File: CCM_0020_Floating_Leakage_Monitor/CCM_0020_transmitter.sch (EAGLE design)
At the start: 61 parts, among them IC1 LMC6041, IC2 LT1494, IC3 LT1495, IC4 LTC1440, IC6 LT6656A-5.0V, Q1 SMP4117A, Q2 SMP4117A, Q3 SMP4117A, Q4 SMP4117A, T1 3904SM

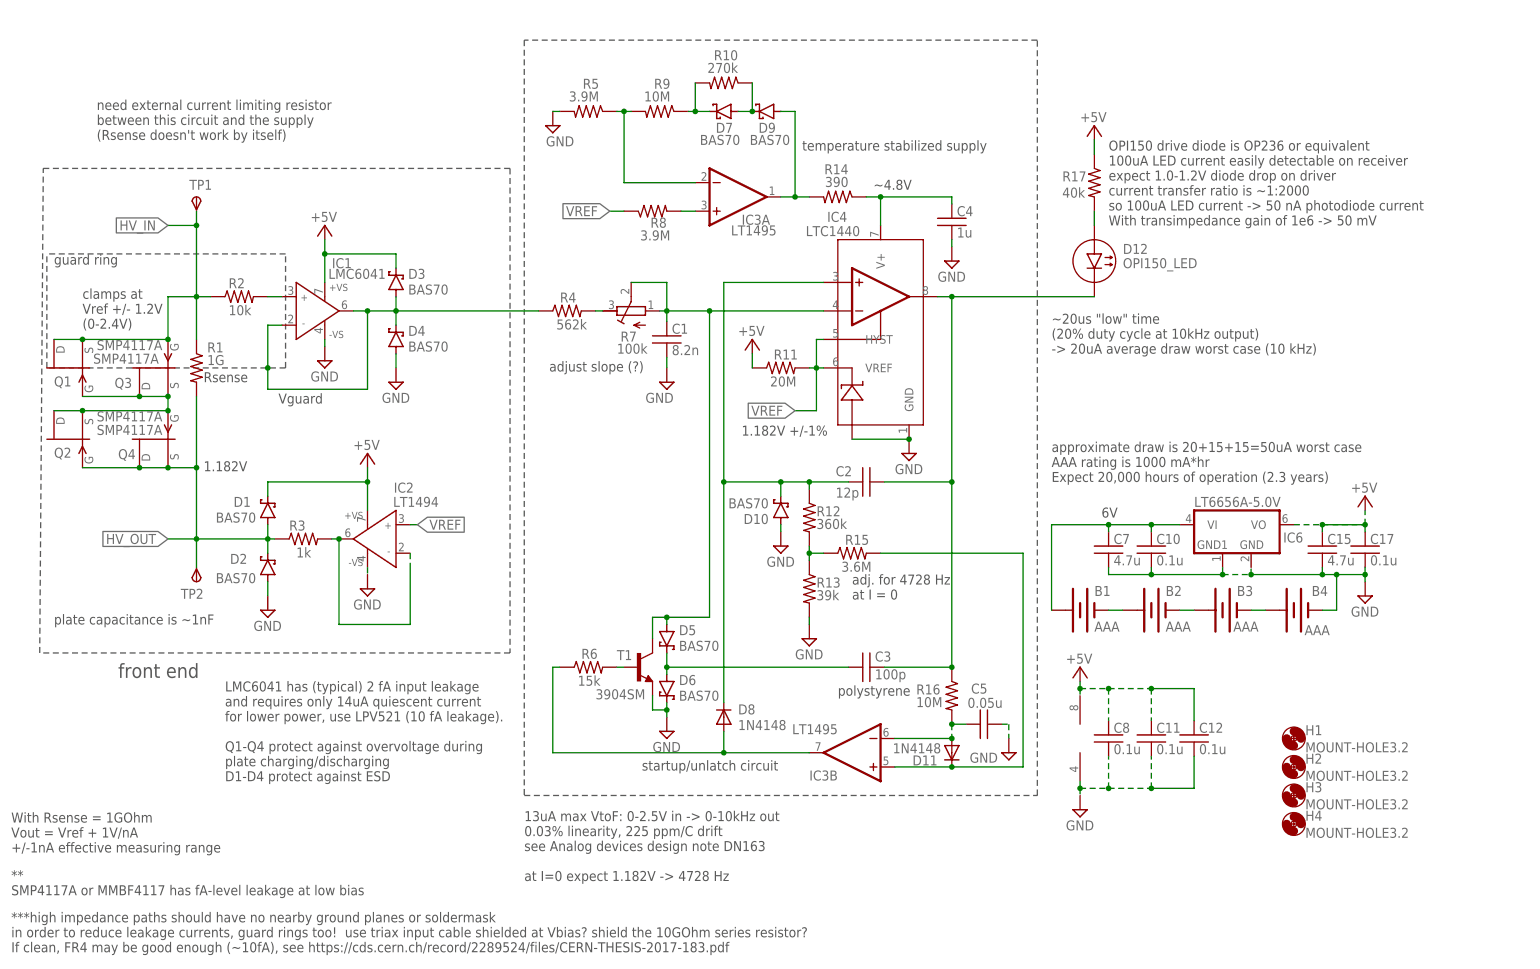
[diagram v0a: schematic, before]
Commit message: CCM_0020 directory organization
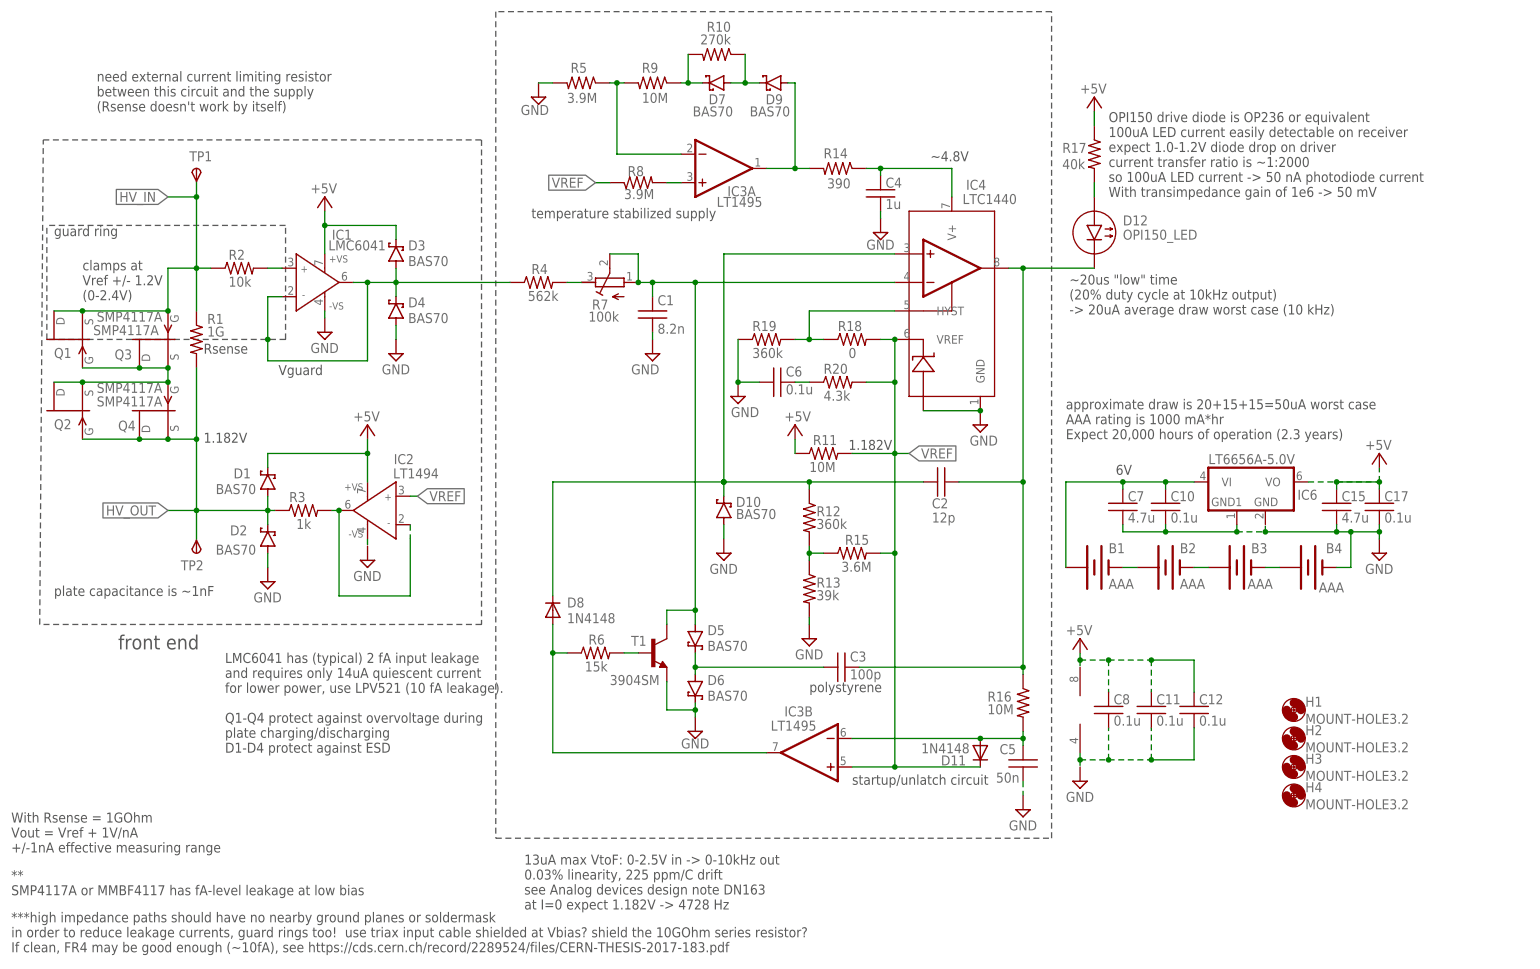
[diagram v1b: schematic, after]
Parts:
- added C6: 0.1u, acrooptics:C0603
- added R18: 0, acrooptics:R0603
- added R19: 360k, acrooptics:R0603
- added R20: 4.3k, acrooptics:R0603
- C5: value 0.05u -> 50n
- R11: value 20M -> 10M
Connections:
- removed net N$17: D11.C, IC3B.+IN, R15.2
- removed net N$21: R8.1
- new net N$2: IC4.HYST, R18.1, R19.2
- new net N$5: C6.2, R20.1
- net GND: now also C6.1, R19.1
- net VREF: now also D11.C, IC3B.+IN, R15.2, R18.2, R20.2, R8.1; no longer IC4.HYST
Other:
- note removed: "1.182V +/-1%"
- note removed: "adj. for 4728 Hz at I = 0"
- note removed: "adjust slope (?)"
- moved on the sheet: B1, B2, B3, B4, C1, C10, C11, C12, C15, C17, C2, C3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
